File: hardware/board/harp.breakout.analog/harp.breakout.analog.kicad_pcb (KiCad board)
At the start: 2 copper layers, 40 x 75 mm, 26 parts, among them J1 Conn_01x12_Socket, J10 Conn_01x01_Pin, J2 Conn_01x03_Pin, J3 Conn_01x03_Pin, J4 Conn_01x03_Pin, J5 Conn_02x10_Odd_Even, J6 Conn_01x03_Pin, J7 Conn_01x03_Pin, J8 Conn_01x03_Pin, J9 Conn_01x01_Pin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

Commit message: Analog Breakout layout
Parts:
- removed J10: Conn_01x01_Pin, Connector_Pin:Pin_D1.0mm_L10.0mm
- removed U5: TXB0108, Package_SO:TSSOP-20_4.4x6.5mm_P0.65mm
- added G***: LOGO, AI_Logos:AI_Petal_8x9, F.Cu at (139.8, 52.8)
- added U3: TXB0104D, Package_SO:SOIC-14_3.9x8.7mm_P1.27mm, B.Cu at (153.5, 80.5)
- J9: value Conn_01x01_Pin -> Conn_01x06_Pin; footprint Connector_Pin:Pin_D1.0mm_L10.0mm -> Connector_PinHeader_2.54mm:PinHeader_1x06_P2.54mm_Vertical
- moved C5 38.2 mm to (156.0, 86.0), turned to -90 degrees
- moved C1 37.8 mm to (149.2, 86.3)
- moved C2 37.8 mm to (150.2, 86.3)
- moved R1 37.7 mm to (158.5, 86.0), turned to -90 degrees
- moved C4 37.4 mm to (149.0, 75.0), turned to 90 degrees
- moved C3 36.0 mm to (150.0, 75.0), turned to -90 degrees
- moved J9 2.55 mm to (133.7, 107.0), turned to 90 degrees
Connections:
- J1 pad 1: /IN3_5V -> /OUT1_5V
- J1 pad 4: /IN2_5V -> /OUT0_5V
- J5 pad 11: /SPI_Out -> /SPI_In
- J5 pad 13: /SPI_In -> /SPI_Out
- J5 pad 5: /IN2 -> /OUT0
- J5 pad 7: /IN3 -> /OUT1
- J9 pad 1: /A6 -> +5V
- U1 pad 14: GNDA -> GND
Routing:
- net +3.3V: track 4.85 -> 150.5 mm, vias 0 -> 2
- net +5V: track 0.00 -> 93.1 mm, vias 2 -> 5
- net /OUT1: track 1.94 -> 49.9 mm
- net /OUT0: track 2.59 -> 50.5 mm
- net /A7: track 0.00 -> 38.5 mm, vias 0 -> 1
- net /A6: track 0.00 -> 38.4 mm, vias 0 -> 1
- net /A5: track 0.00 -> 30.5 mm
- net /OUT0_5V: track 1.61 -> 27.4 mm
- net /IN2: track 24.3 -> 0.00 mm
- net /IN1: track 27.3 -> 51.4 mm
- net /IN0: track 30.7 -> 53.0 mm
- net /OUT1_5V: track 5.43 -> 27.5 mm
- net /IN2_5V: track 22.0 -> 0.00 mm
- net /IN3: track 21.9 -> 0.00 mm
- net GND: track 3.51 -> 17.5 mm, vias 4 -> 8
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- added copper zone on F.Cu, net +5V
- removed copper zone on B.Cu, net +5V
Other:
- board text added: "0368"
- board text added: "22"
- board text added: "23"
- board text added: "24"
- board text added: "25"
- board text added: "3V3"
- board text added: "5V logic input/output connected devices using pullups, >50KOhm compatible: 3M Mini Clamp Socket Series 37103-2165-000 FL 100 37103-3101-000 FL 100"
- board text added: "<CAM0"
- board text added: "<CAM1"
- board text added: "<Poke"
- board text added: "A6"
- board text added: "A7"
- board text added: "G"
- board text added: "IO"
- board text added: "N Mars 3.12.26 0368 Analog Breakout"
- board text removed: "0368-E-002-001.000.000"
- board text removed: "AUX GPIO Breakout"
- board text removed: "GPIO"
- board text removed: "Sonya Vasquez Mar 3, 2025"
- board text removed: "· 5V logic input/output. · connected devices using pullups must use pullups >50KOhm. · compatible connectors: 3M Mini Clamp Socket Series. · 37103-2165-000 FL 100 · 37103-3101-000 FL 100"

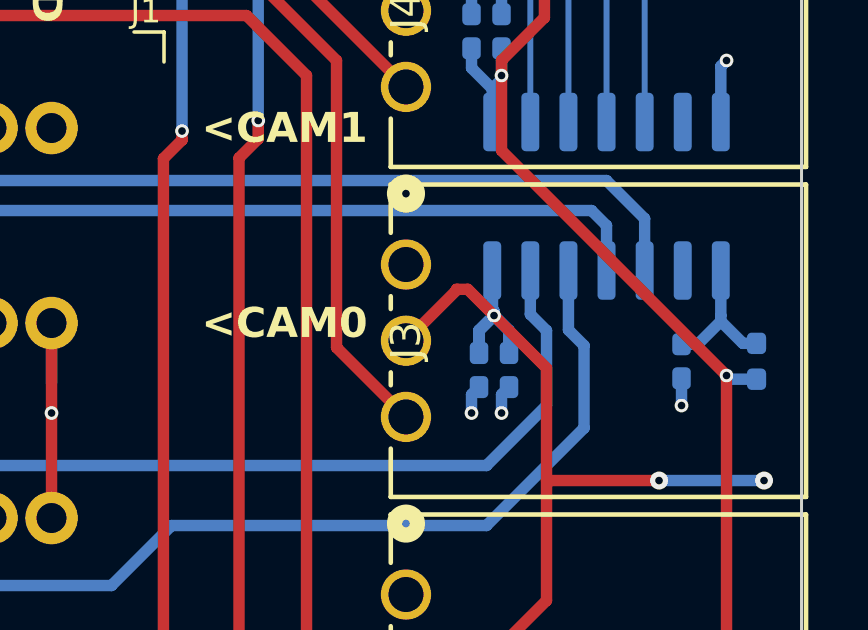
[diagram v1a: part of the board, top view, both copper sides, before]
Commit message: Minor analog board silk updates
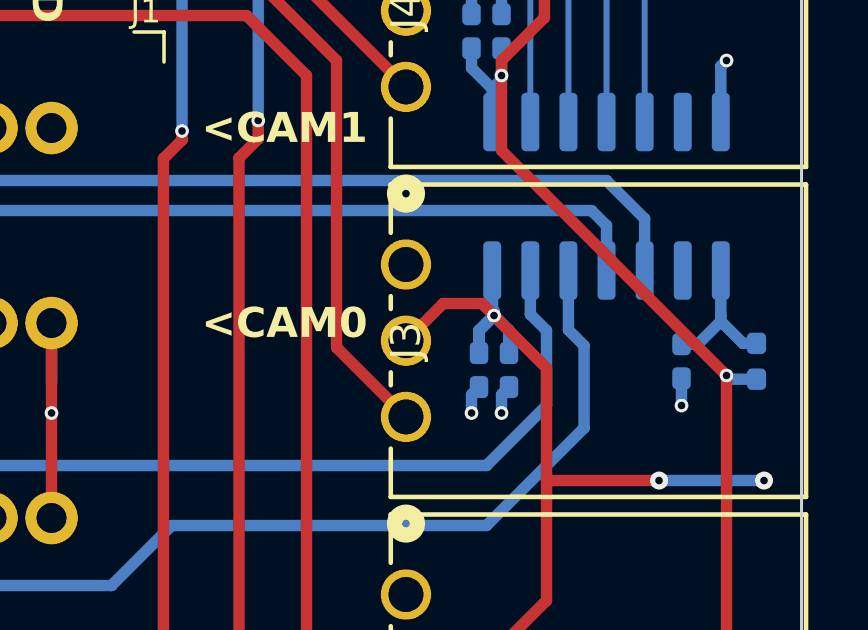
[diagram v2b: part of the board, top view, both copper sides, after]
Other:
- board text added: "+5V"
- board text added: "SIG (0-3.3V)"
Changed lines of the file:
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@@
+		)
+	)
+	(gr_text "+5V"
+		(at 131.1 52.7 0)
+		(layer "B.SilkS")
+		(effects
+			(font
+				(size 1 1)
+				(thickness 0.2)
+				(bold yes)
+			)
+			(justify left mirror)
 		)
 	)
@@
 		)
 	)
+	(gr_text "SIG (0-3.3V)"
+		(at 131.1 50.2 0)
+		(layer "B.SilkS")
+		(effects
+			(font
+				(size 1 1)
+				(thickness 0.2)
+				(bold yes)
+			)
+			(justify left mirror)
+		)
+	)
 	(gr_text "GPIO25"
 		(at 137.392 48.2 90)
@@
 		)
 	)
+	(gr_text "GND"
+		(at 131.1 55.2 0)
+		(layer "B.SilkS")
+		(effects
+			(font
+				(size 1 1)
+				(thickness 0.2)
+				(bold yes)
+			)
+			(justify left mirror)
+		)
+	)
+	(gr_text "+5V"
+		(at 148.8 63.3 180)
+		(layer "B.SilkS")
+		(effects
+			(font
+				(size 1 1)
+				(thickness 0.2)
+				(bold yes)
+			)
+			(justify left mirror)
+		)
+	)
+	(gr_text "+5V"
+		(at 148.5 96.4 180)
+		(layer "B.SilkS")
+		(effects
+			(font
+				(size 1 1)
+				(thickness 0.2)
+				(bold yes)
+			)
+			(justify left mirror)
+		)
+	)
 	(gr_text "5V logic input/output\nconnected devices using pullups, >50KOhm\ncompatible: 3M Mini Clamp Socket Series\n  37103-2165-000 FL 100\n  37103-3101-000 FL 100"
 		(at 144.25 71 90)
@@
 		)
 	)
+	(gr_text "GND"
+		(at 148.8 60.8 180)
+		(layer "B.SilkS")
+		(effects
+			(font
+				(size 1 1)
+				(thickness 0.2)
+				(bold yes)
+			)
+			(justify left mirror)
+		)
+	)
 	(gr_text "GPIO27"
 		(at 142.492 48.2 90)
@@
 		)
 	)
+	(gr_text "SIG (0-3.3V)"
+		(at 148.5 98.9 180)
+		(layer "B.SilkS")
+		(effects
+			(font
+				(size 1 1)
+				(thickness 0.2)
+				(bold yes)
+			)
+			(justify left mirror)
+		)
+	)
 	(gr_text "GPIO29"
 		(at 147.592 48.2 90)
@@
 		)
 	)
+	(gr_text "GND"
+		(at 148.5 93.9 180)
+		(layer "B.SilkS")
+		(effects
+			(font
+				(size 1 1)
+				(thickness 0.2)
+				(bold yes)
+			)
+			(justify left mirror)
+		)
+	)
 	(gr_text "GPIO24"
 		(at 134.892 48.2 90)
@@
 		)
 	)
+	(gr_text "SIG (0-3.3V)"
+		(at 148.8 65.8 180)
+		(layer "B.SilkS")
+		(effects
+			(font
+				(size 1 1)
+				(thickness 0.2)
+				(bold yes)
+			)
+			(justify left mirror)
+		)
+	)
 	(segment
 		(start 149 72.154193)
@@
 	)
 	(segment
-		(start 148.5 83.625)
-		(end 148.5 83.654193)
+		(start 149.75 84.5)
+		(end 149.35 84.1)
 		(width 0.381)
 		(layer "F.Cu")
@@
 	)
 	(segment
-		(start 148.5 83.654193)
-		(end 146.814593 85.3396)
-		(width 0.381)
-		(layer "F.Cu")
-		(net 1)
-	)
-	(segment
 		(start 151.5 90)
 		(end 151.5 94)
@@
 	)
 	(segment
+		(start 148.054193 84.1)
+		(end 146.814593 85.3396)
+		(width 0.381)
+		(layer "F.Cu")
+		(net 1)
+	)
+	(segment
 		(start 148.8396 63.3396)
 		(end 149 63.5)
@@
 	)
 	(segment
-		(start 148.875 83.625)
-		(end 148.5 83.625)
-		(width 0.381)
-		(layer "F.Cu")
-		(net 1)
-	)
-	(segment
 		(start 146.814593 63.3396)
 		(end 148.8396 63.3396)
@@
 	)
 	(segment
-		(start 149.75 84.5)
-		(end 148.875 83.625)
-		(width 0.381)
-		(layer "F.Cu")
+		(start 149.35 84.1)
+		(end 148.054193 84.1)
+		(width 0.381)
+		(layer "F.Cu")

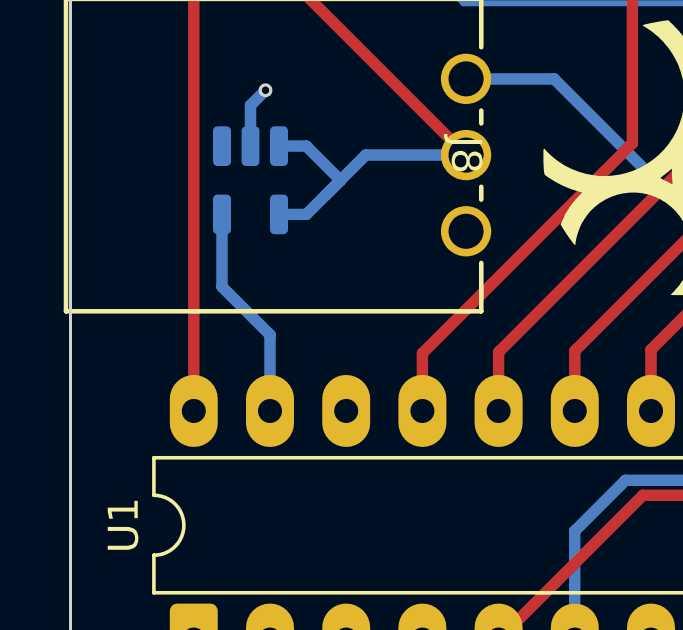
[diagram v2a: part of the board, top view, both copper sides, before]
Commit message: Added bypass caps and updated BOM
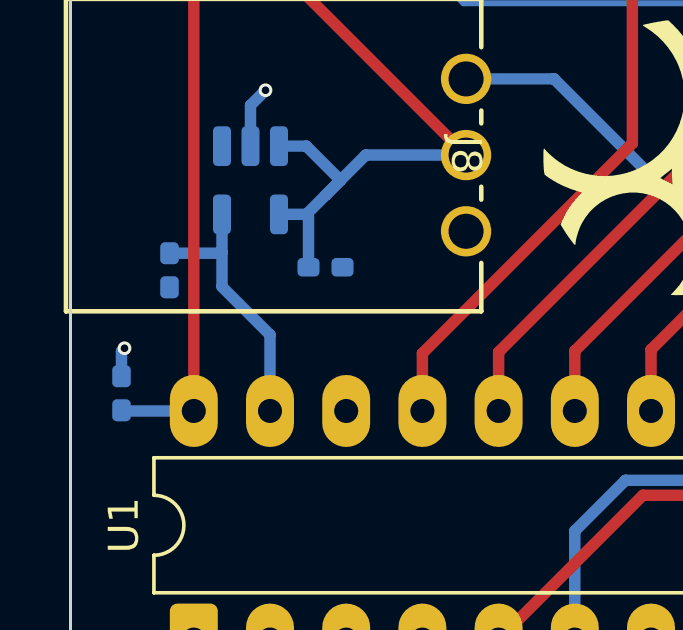
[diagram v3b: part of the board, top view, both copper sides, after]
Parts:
- added C6: 1uF, Capacitor_SMD:C_0402_1005Metric_Pad0.74x0.62mm_HandSolder, B.Cu at (121.7, 60.6)
- added C7: 0.1uF, Capacitor_SMD:C_0402_1005Metric_Pad0.74x0.62mm_HandSolder, B.Cu at (128.5, 56.4)
- added C8: 0.1uF, Capacitor_SMD:C_0402_1005Metric_Pad0.74x0.62mm_HandSolder, B.Cu at (123.3, 56.5)
- U1: value MCP3008 -> MCP3208
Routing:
- net +3.3V: track 150.5 -> 152.9 mm
- net +5V: track 92.6 -> 94.4 mm
- net /3.3VRef: track 7.22 -> 8.98 mm
- net GND: track 17.5 -> 18.4 mm, vias 8 -> 9

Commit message: Rebuild GND plane
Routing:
- net GND: track 18.4 -> 10.6 mm, vias 9 -> 2
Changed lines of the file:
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@@
-	)
-	(via
-		(at 157.5 76)
-		(size 0.4572)
-		(drill 0.254)
-		(layers "F.Cu" "B.Cu")
-		(net 2)
-	)
-	(via
-		(at 150 73.5)
-		(size 0.4572)
-		(drill 0.254)
-		(layers "F.Cu" "B.Cu")
-		(net 2)
 	)
 	(via
@@
 	)
 	(via
-		(at 156 87.5)
-		(size 0.4572)
-		(drill 0.254)
-		(layers "F.Cu" "B.Cu")
-		(net 2)
-	)
-	(via
-		(at 149 73.5)
-		(size 0.4572)
-		(drill 0.254)
-		(layers "F.Cu" "B.Cu")
-		(net 2)
-	)
-	(via
 		(at 126.5 50.5)
 		(size 0.4572)
@@
 		(net 2)
 	)
-	(via
-		(at 150 87.75)
-		(size 0.4572)
-		(drill 0.254)
-		(layers "F.Cu" "B.Cu")
-		(net 2)
-	)
-	(via
-		(at 121.8 59.1)
-		(size 0.4572)
-		(drill 0.254)
-		(layers "F.Cu" "B.Cu")
-		(net 2)
-	)
-	(via
-		(at 149 87.75)
-		(size 0.4572)
-		(drill 0.254)
-		(layers "F.Cu" "B.Cu")
-		(net 2)
-	)
-	(segment
-		(start 121.7 59.2)
-		(end 121.8 59.1)
-		(width 0.381)
-		(layer "B.Cu")
-		(net 2)
-	)
-	(segment
-		(start 121.7 60.0325)
-		(end 121.7 59.2)
-		(width 0.381)
-		(layer "B.Cu")
-		(net 2)
-	)
 	(segment
 		(start 126 52.3625)
@@
 	)
 	(segment
-		(start 157.31 76.19)
-		(end 157.5 76)
-		(width 0.381)
-		(layer "B.Cu")
-		(net 2)
-	)
-	(segment
 		(start 135 84.75)
 		(end 135 86.75)
@@
 	)
 	(segment
-		(start 149 87.135)
-		(end 149 87.75)
-		(width 0.381)
-		(layer "B.Cu")
-		(net 2)
-	)
-	(segment
 		(start 126 51)
 		(end 126.5 50.5)
-		(width 0.381)
-		(layer "B.Cu")
-		(net 2)
-	)
-	(segment
-		(start 150 74.4575)
-		(end 150 73.5)
-		(width 0.381)
-		(layer "B.Cu")
-		(net 2)
-	)
-	(segment
-		(start 150.25 86.885)
-		(end 150 87.135)
-		(width 0.381)
-		(layer "B.Cu")
-		(net 2)
-	)
-	(segment
-		(start 150 87.135)
-		(end 150 87.75)
-		(width 0.381)
-		(layer "B.Cu")
-		(net 2)
-	)
-	(segment
-		(start 156 87.5)
-		(end 156 86.5925)
-		(width 0.381)
-		(layer "B.Cu")
-		(net 2)
-	)
-	(segment
-		(start 149 74.4575)
-		(end 149 73.5)
-		(width 0.381)
-		(layer "B.Cu")
-		(net 2)
-	)
-	(segment
-		(start 157.31 78.05)
-		(end 157.31 76.19)
-		(width 0.381)
-		(layer "B.Cu")
-		(net 2)
-	)
-	(segment
-		(start 149.25 86.885)
-		(end 149 87.135)
 		(width 0.381)
 		(layer "B.Cu")
@@
 	)
 	(segment
-		(start 151.5 85)
-		(end 151.5 87.5)
-		(width 0.381)
-		(layer "B.Cu")
-		(net 10)
-	)
-	(segment
 		(start 150.96 83)
 		(end 150.96 84.46)
@@
 	)
 	(segment
+		(start 150.96 84.46)
+		(end 151.5 85)
+		(width 0.381)
+		(layer "B.Cu")
+		(net 10)
+	)
+	(segment
+		(start 149.9 89.5)
+		(end 129 89.5)
+		(width 0.381)
+		(layer "B.Cu")
+		(net 10)
+	)
+	(segment
 		(start 128.5 90)
 		(end 128.5 95.25)
@@
 	)
 	(segment
-		(start 150.96 84.46)
-		(end 151.5 85)
-		(width 0.381)
-		(layer "B.Cu")
-		(net 10)
-	)
-	(segment
-		(start 151.5 87.5)
-		(end 149.5 89.5)
-		(width 0.381)
-		(layer "B.Cu")
-		(net 10)
-	)
-	(segment
-		(start 149.5 89.5)
-		(end 129 89.5)
-		(width 0.381)
-		(layer "B.Cu")
-		(net 10)
-	)
-	(segment
 		(start 128.5 95.25)
 		(end 131 97.75)
+		(width 0.381)
+		(layer "B.Cu")
+		(net 10)
+	)
+	(segment
+		(start 151.5 85)
+		(end 151.5 87.9)
+		(width 0.381)
+		(layer "B.Cu")
+		(net 10)
+	)
+	(segment
+		(start 151.5 87.9)
+		(end 149.9 89.5)
 		(width 0.381)
 		(layer "B.Cu")
@@
 		(layer "B.Cu")
 		(hatch edge 0.5)
-		(connect_pads yes
+		(connect_pads
 			(clearance 0.4)
 		)

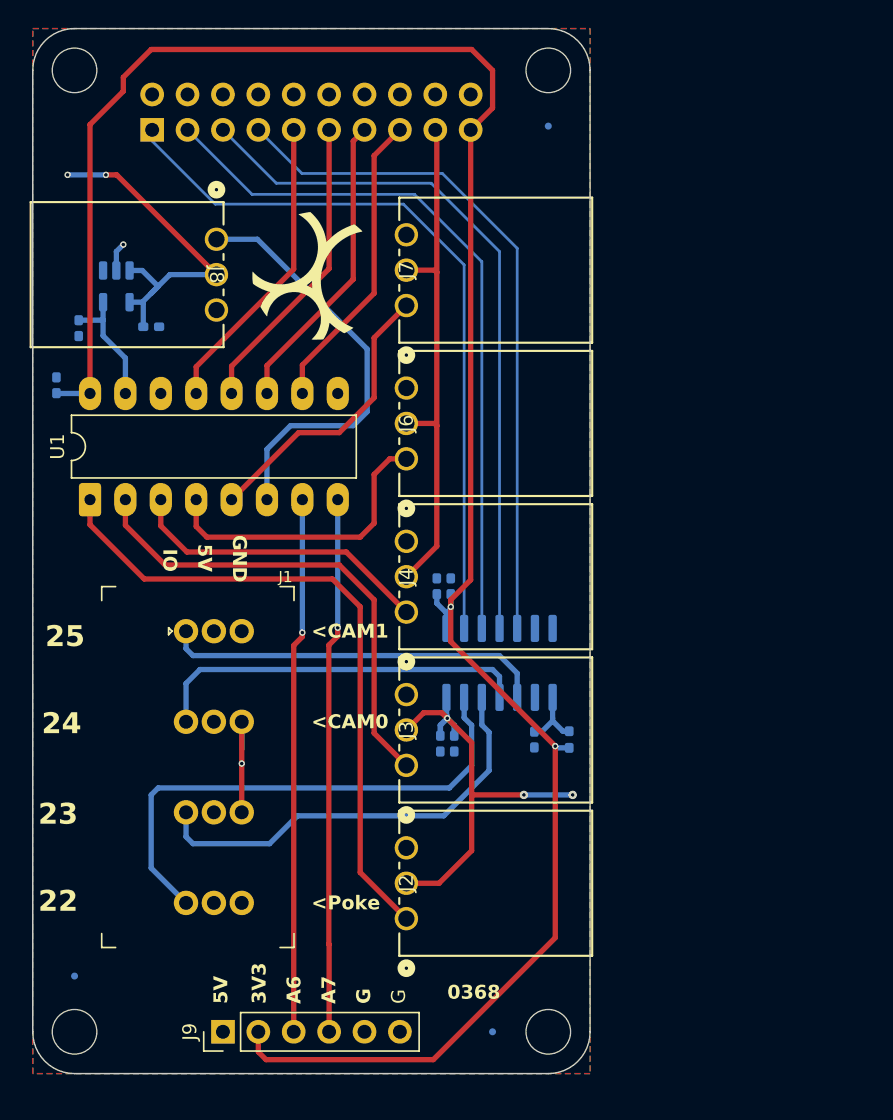
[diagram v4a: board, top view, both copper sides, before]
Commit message: Improved silkscreen and corrected SPI pins
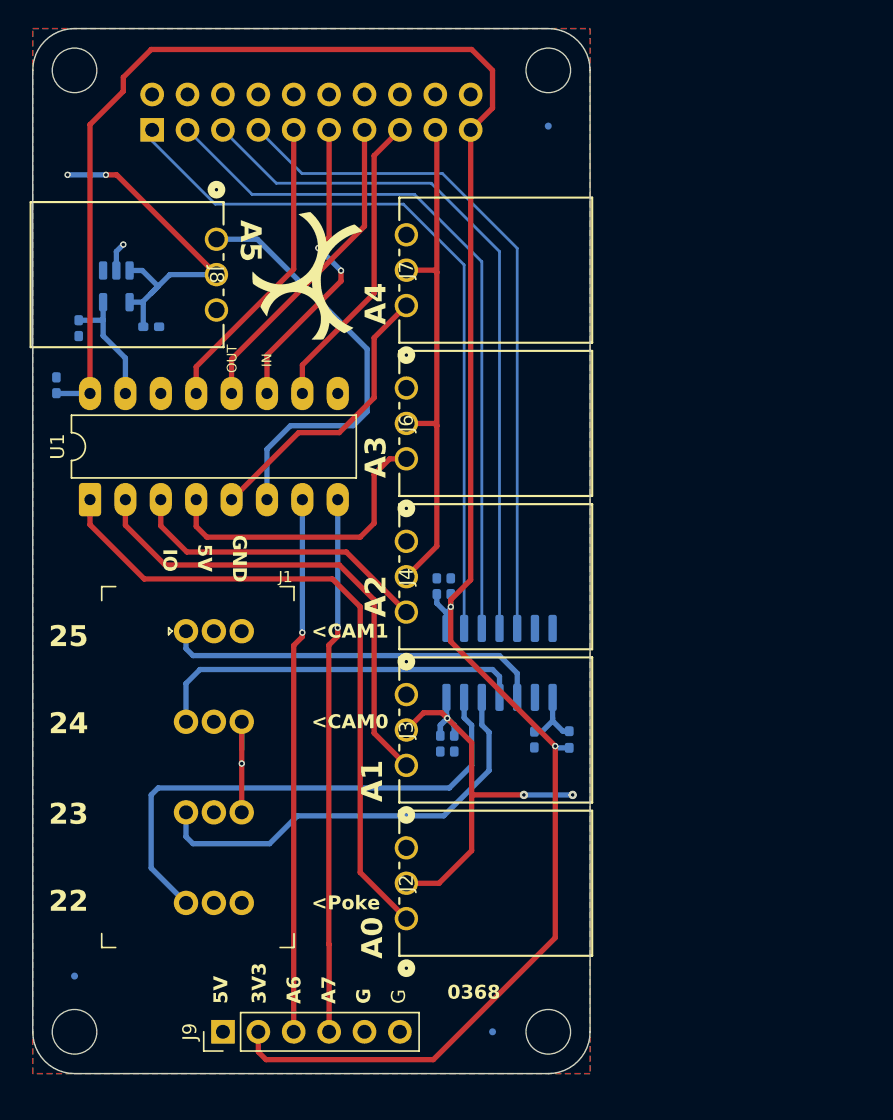
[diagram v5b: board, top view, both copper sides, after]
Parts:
- C7, C8: value 0.1uF -> 100nF
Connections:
- U1 pad 11: /SPI_Out -> /SPI_In
- U1 pad 12: /SPI_In -> /SPI_Out
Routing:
- net /SPI_Out: track 22.3 -> 23.3 mm
- net /SPI_In: track 22.2 -> 22.5 mm, vias 0 -> 2
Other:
- board text added: "A0"
- board text added: "A1"
- board text added: "A2"
- board text added: "A3"
- board text added: "A4"
- board text added: "A5"
- board text added: "IN"
- board text added: "N Mars 4.14.26 0368 Analog Breakout"
- board text added: "OUT"
- board text removed: "N Mars 3.12.26 0368 Analog Breakout"
